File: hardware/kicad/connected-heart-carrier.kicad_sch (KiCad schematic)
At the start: 18 parts, among them J1 TOUCH, J2 LED, J3 EPD, SW1 RESET, U1 ESP32-C3 SuperMini, U2 74AHCT1G125

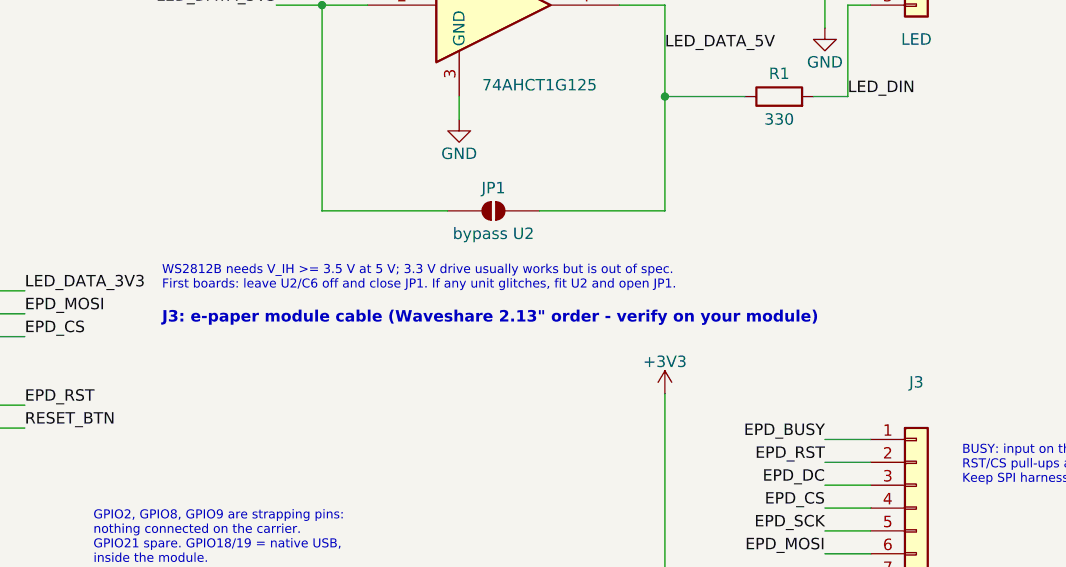
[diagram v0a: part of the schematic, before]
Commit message: Schematic: fit U2, leave JP1 open
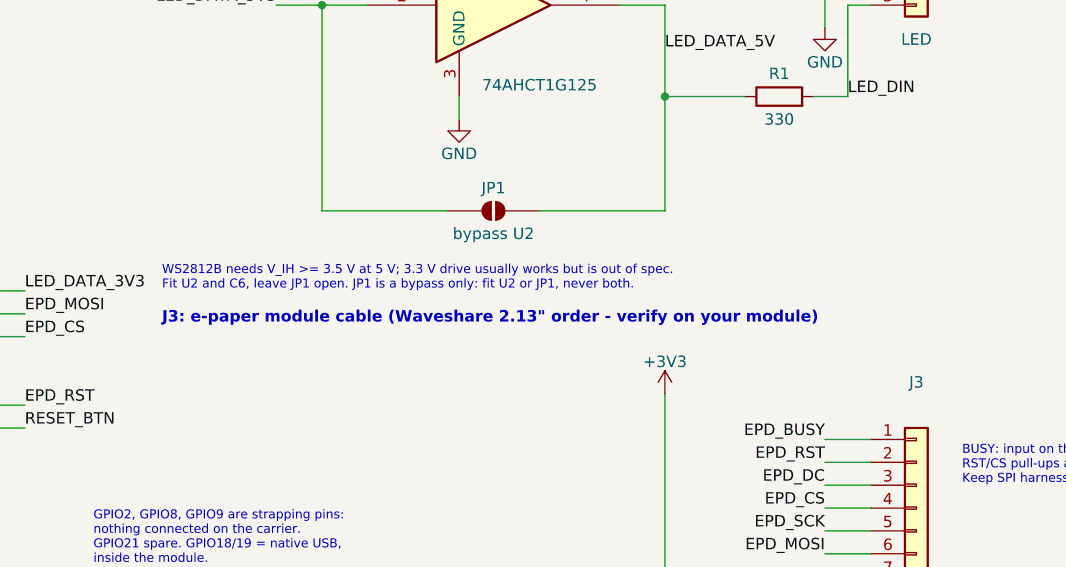
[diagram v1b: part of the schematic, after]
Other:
- note added: "WS2812B needs V_IH >= 3.5 V at 5 V; 3.3 V drive usually works but is out of spec. Fit U2 and C6, leave JP1 open. JP1 is a bypass only: fit U2 or JP1, never both."
- note removed: "WS2812B needs V_IH >= 3.5 V at 5 V; 3.3 V drive usually works but is out of spec. First boards: leave U2/C6 off and close JP1. If any unit glitches, fit U2 and open JP1."
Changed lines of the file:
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@@
 		)
 	)
-	(text "WS2812B needs V_IH >= 3.5 V at 5 V; 3.3 V drive usually works but is out of spec.\nFirst boards: leave U2/C6 off and close JP1. If any unit glitches, fit U2 and open JP1."
+	(text "WS2812B needs V_IH >= 3.5 V at 5 V; 3.3 V drive usually works but is out of spec.\nFit U2 and C6, leave JP1 open. JP1 is a bypass only: fit U2 or JP1, never both."
 		(exclude_from_sim no)
 		(at 139.7 92.71 0)
